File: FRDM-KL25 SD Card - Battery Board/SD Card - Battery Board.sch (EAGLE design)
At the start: 64 parts, among them J3 SSW-108-02-S-D, J4 SSW-110-02-S-D, J5 SSW-108-02-S-D, J6 SSW-106-02-S-D, U1 TPS63001, U2 TPS63002, U3 BQ27510DRZT-G3, U4 BQ24210DQCT

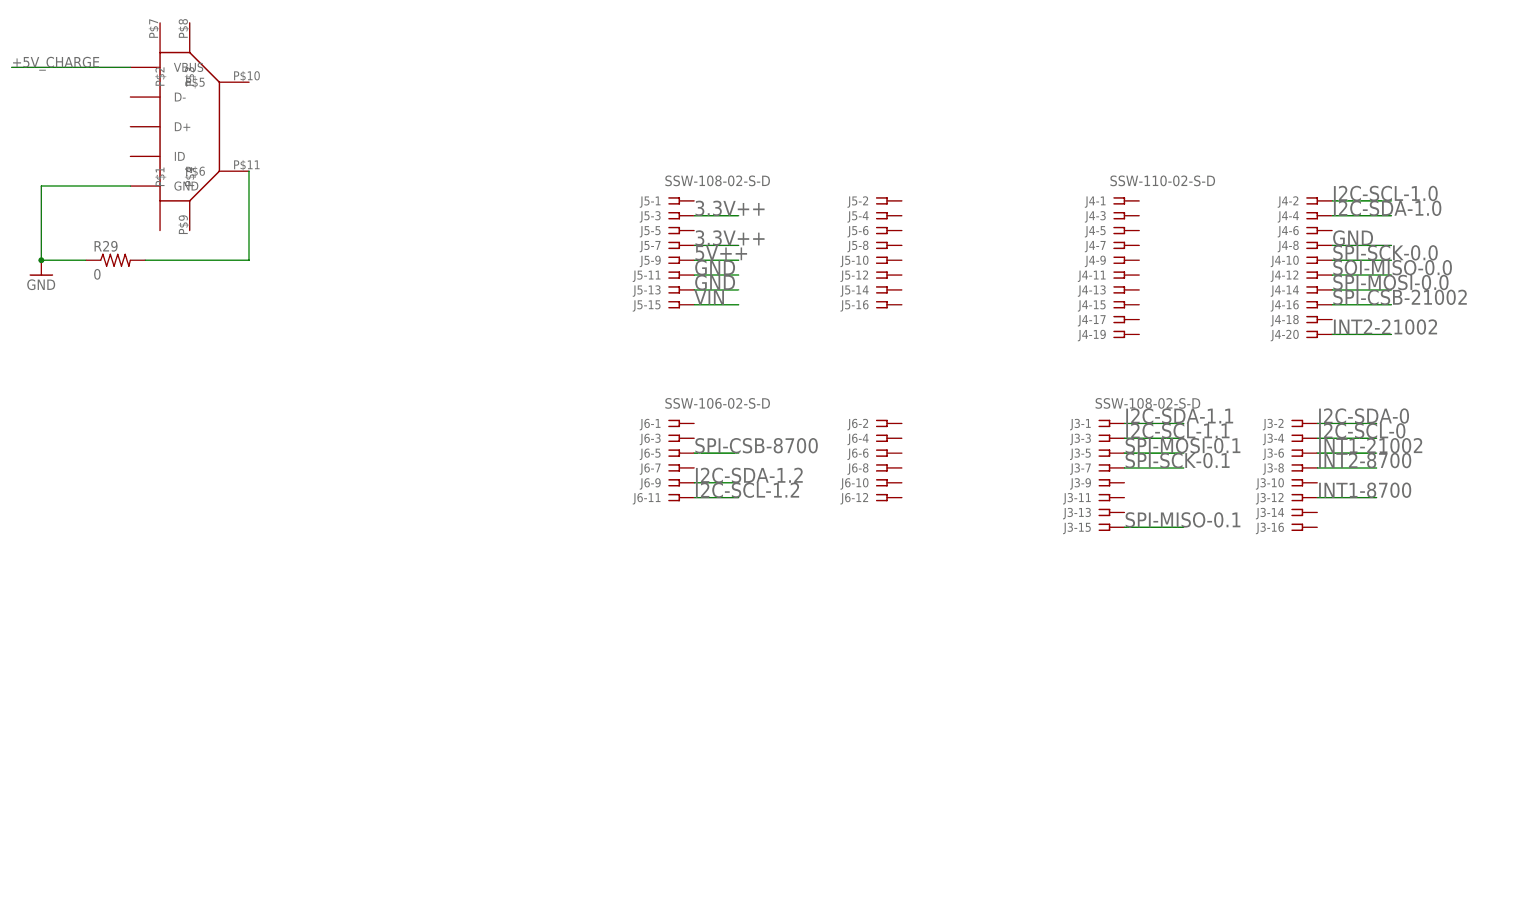
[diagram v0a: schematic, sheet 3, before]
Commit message: FRDM-KL25Z: LED names were updated to refelect the correct color, Layout of page 3 schematics was rearranged for better clarity. The the PCB the location of the SD card was placed in teh center, USB receptical was also placed in its needed location, SD card pull up resistors have been placed and connected, vias with 0.1 inch spacing have been used to ficilitate a header or test pins should that be needed.
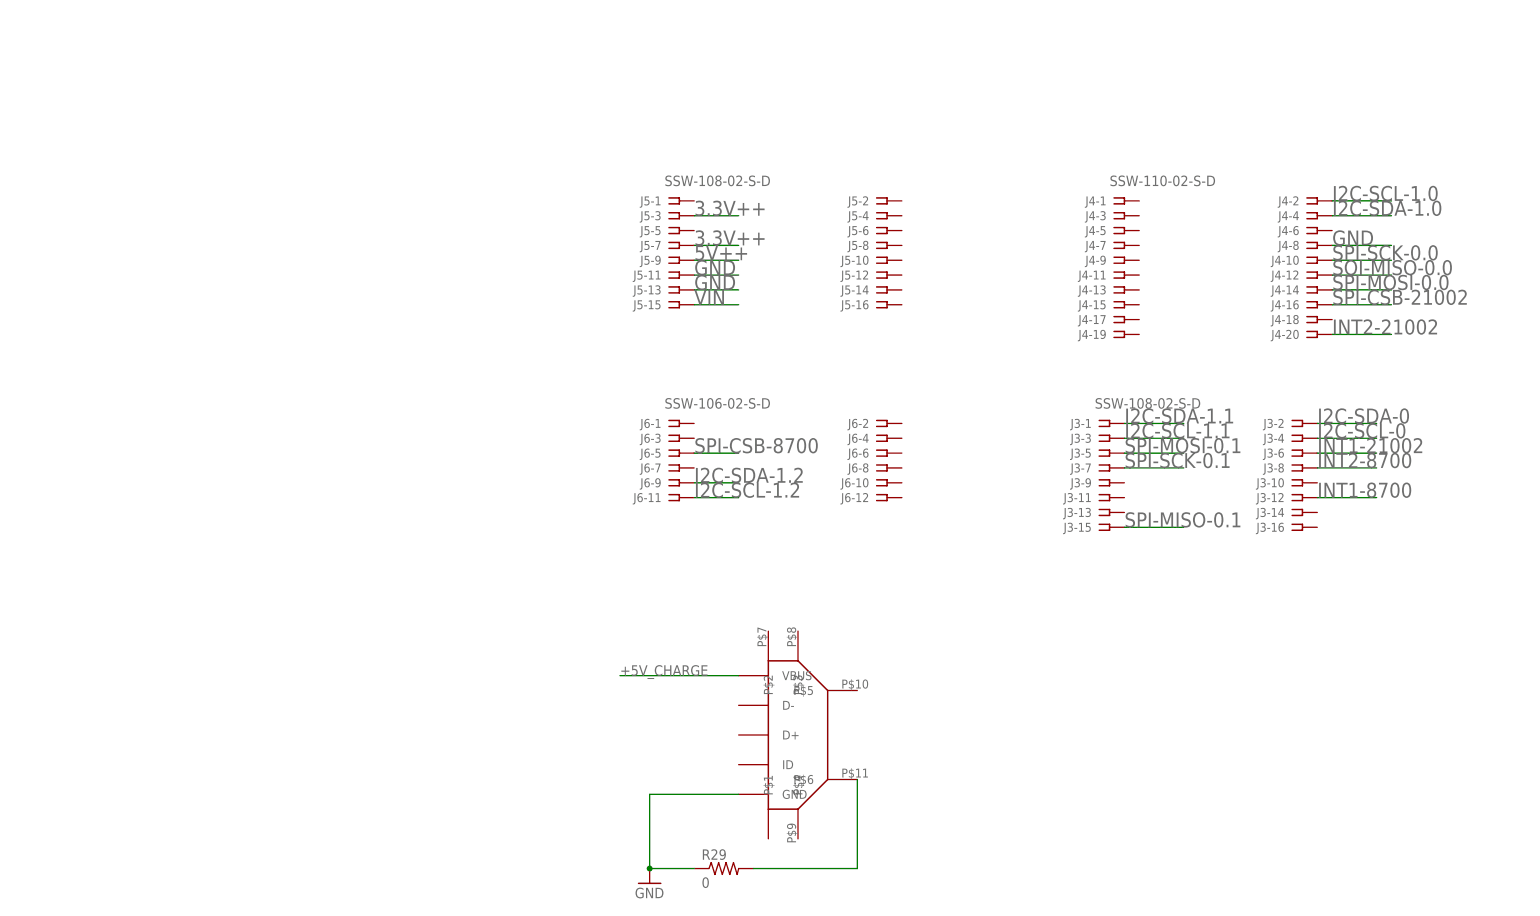
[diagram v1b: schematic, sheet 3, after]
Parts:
- D1: value Blue-LED -> Red-LED
- D2: value Green-LED -> Yellow-LED
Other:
- moved on the sheet: R29
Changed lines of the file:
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@@
 <part name="R12" library="Kas-Resistors" deviceset="RESISTOR" device="10K-62.5M-1%-50V" value="10k"/>
 <part name="R13" library="Kas-Resistors" deviceset="RESISTOR" device="10K-62.5M-1%-50V" value="10k"/>
-<part name="D2" library="Kas-Diodes-LEDs" deviceset="0.8X1.2" device="GREEN-3.3V-20M" value="Green-LED"/>
+<part name="D2" library="Kas-Diodes-LEDs" deviceset="0.8X1.2" device="GREEN-3.3V-20M" value="Yellow-LED"/>
 <part name="R14" library="Kas-Resistors" deviceset="RESISTOR" device="1K-63M-1%-50V-0402" value="1k"/>
 <part name="GND2" library="supply1" deviceset="GND" device=""/>
@@
 <part name="R25" library="Kas-Resistors" deviceset="RESISTOR" device="10K-62.5M-1%-50V" value="10k"/>
 <part name="R26" library="Kas-Resistors" deviceset="RESISTOR" device="1K-63M-1%-50V-0402" value="1k"/>
-<part name="D1" library="Kas-Diodes-LEDs" deviceset="0.8X1.2" device="BLUE-3.3V-20M" value="Blue-LED"/>
+<part name="D1" library="Kas-Diodes-LEDs" deviceset="0.8X1.2" device="BLUE-3.3V-20M" value="Red-LED"/>
 <part name="J1" library="Kas-Connectors" deviceset="SD_CARD_SLOT" device=""/>
 <part name="C2" library="Kas-Capacitors" deviceset="CAPACITOR" device="10U-X5R-20%-6.3V-0402" value="10uF"/>
@@
 <description>Connectors</description>
 <plain>
-<text x="76.2" y="-43.18" size="2.54" layer="101" ratio="14">NEED TO ADD BATTERY CONNECTION</text>
-<text x="190.5" y="30.48" size="2.54" layer="101" ratio="14">NEED TO ADD BATTERY CONNECTION</text>
-<text x="-68.58" y="35.56" size="2.54" layer="101" ratio="14">NEED TO ADD BATTERY CONNECTION</text>
-<text x="66.04" y="124.46" size="2.54" layer="101" ratio="14">NEED TO ADD BATTERY CONNECTION</text>
+<text x="-5.08" y="-38.1" size="2.54" layer="101" ratio="14">NEED TO ADD BATTERY CONNECTION</text>
+<text x="187.96" y="-38.1" size="2.54" layer="101" ratio="14">NEED TO ADD BATTERY CONNECTION</text>
+<text x="190.5" y="124.46" size="2.54" layer="101" ratio="14">NEED TO ADD BATTERY CONNECTION</text>
+<text x="7.62" y="127" size="2.54" layer="101" ratio="14">NEED TO ADD BATTERY CONNECTION</text>
 </plain>
 <instances>
@@
 <instance part="J6" gate="-11" x="50.8" y="45.72"/>
 <instance part="J6" gate="-12" x="86.36" y="45.72"/>
-<instance part="J2" gate="G$1" x="-27.94" y="111.76"/>
-<instance part="R29" gate="G$1" x="-45.72" y="86.36"/>
-<instance part="GND16" gate="1" x="-58.42" y="83.82"/>
+<instance part="J2" gate="G$1" x="76.2" y="7.62"/>
+<instance part="R29" gate="G$1" x="58.42" y="-17.78"/>
+<instance part="GND16" gate="1" x="45.72" y="-20.32"/>
 </instances>
 <busses>
@@
 <pinref part="J2" gate="G$1" pin="GND"/>
 <pinref part="GND16" gate="1" pin="GND"/>
-<wire x1="-43.18" y1="99.06" x2="-58.42" y2="99.06" width="0.1524" layer="91"/>
-<wire x1="-58.42" y1="99.06" x2="-58.42" y2="86.36" width="0.1524" layer="91"/>
-<wire x1="-50.8" y1="86.36" x2="-58.42" y2="86.36" width="0.1524" layer="91"/>
-<junction x="-58.42" y="86.36"/>
+<wire x1="60.96" y1="-5.08" x2="45.72" y2="-5.08" width="0.1524" layer="91"/>
+<wire x1="45.72" y1="-5.08" x2="45.72" y2="-17.78" width="0.1524" layer="91"/>
+<wire x1="53.34" y1="-17.78" x2="45.72" y2="-17.78" width="0.1524" layer="91"/>
+<junction x="45.72" y="-17.78"/>
 <pinref part="R29" gate="G$1" pin="1"/>
 </segment>
@@
 <segment>
 <pinref part="J2" gate="G$1" pin="VBUS"/>
-<wire x1="-43.18" y1="119.38" x2="-63.5" y2="119.38" width="0.1524" layer="91"/>
-<label x="-63.5" y="119.38" size="1.778" layer="95"/>
+<wire x1="60.96" y1="15.24" x2="40.64" y2="15.24" width="0.1524" layer="91"/>
+<label x="40.64" y="15.24" size="1.778" layer="95"/>
 </segment>
 </net>
@@
 <segment>
 <pinref part="J2" gate="G$1" pin="P$6"/>
-<wire x1="-22.86" y1="101.6" x2="-22.86" y2="86.36" width="0.1524" layer="91"/>
-<wire x1="-22.86" y1="86.36" x2="-40.64" y2="86.36" width="0.1524" layer="91"/>
+<wire x1="81.28" y1="-2.54" x2="81.28" y2="-17.78" width="0.1524" layer="91"/>
+<wire x1="81.28" y1="-17.78" x2="63.5" y2="-17.78" width="0.1524" layer="91"/>
 <pinref part="R29" gate="G$1" pin="2"/>
 </segment>

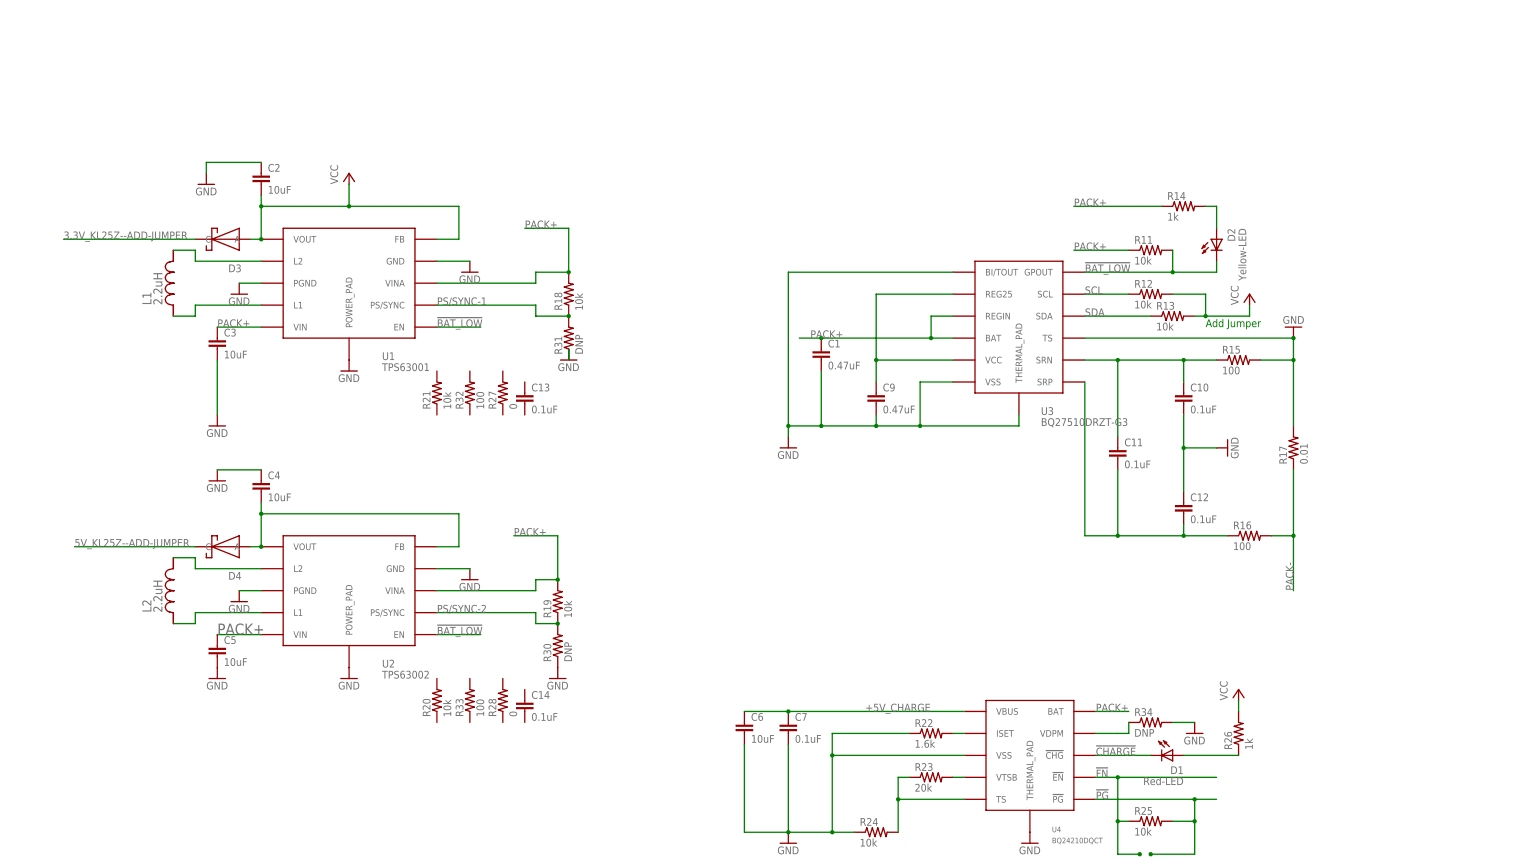
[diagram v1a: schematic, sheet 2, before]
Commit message: FRDM-KL26Z: Added 5V+ and changed VCC to 3V3+, moved battery section off PCB in preperation for branch
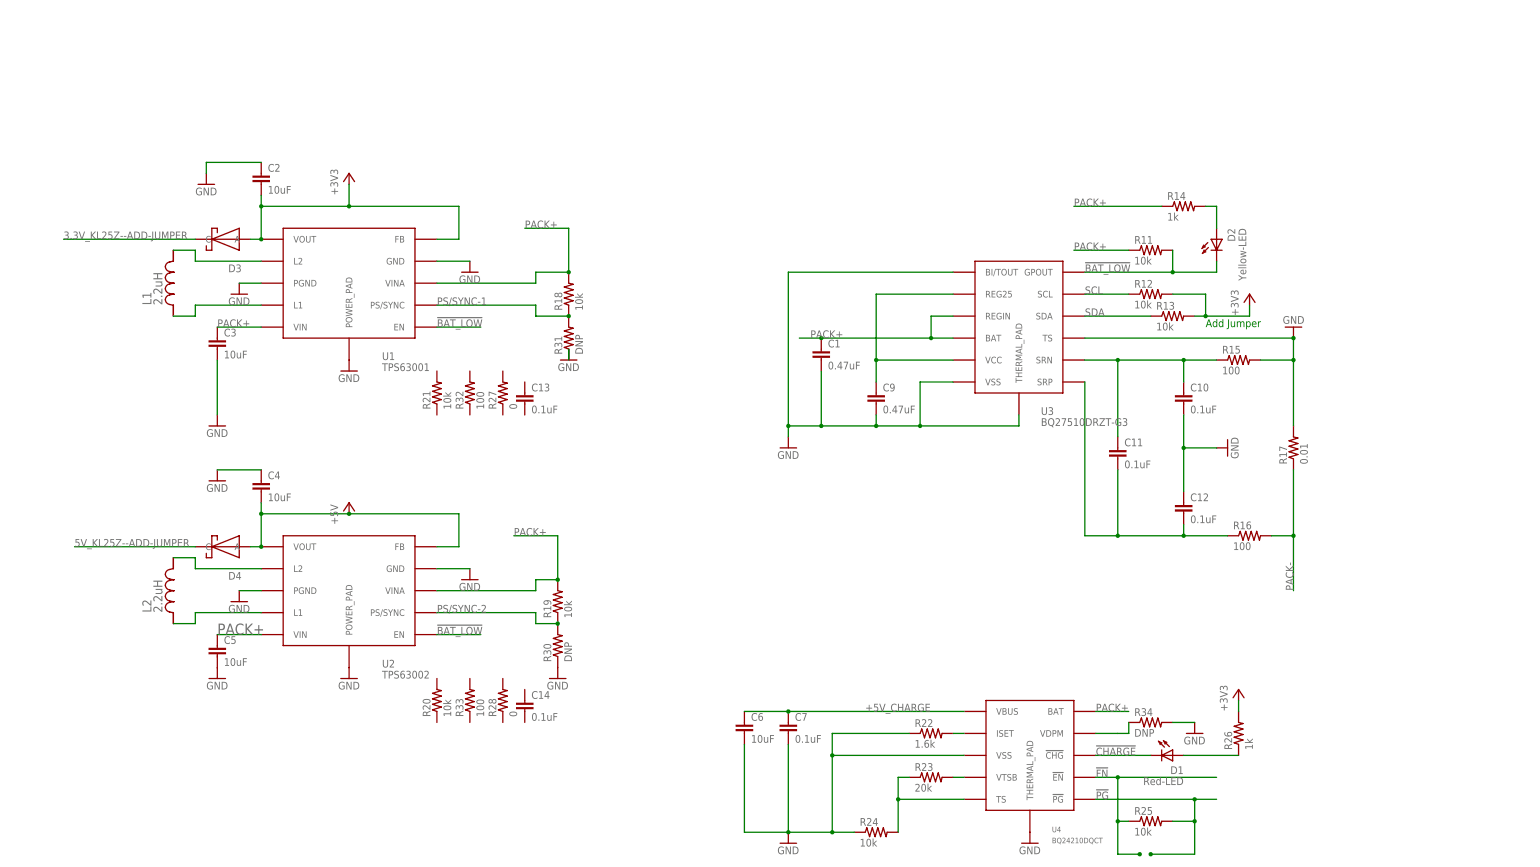
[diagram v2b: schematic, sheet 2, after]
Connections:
- net N$2 renamed +5V
- net VCC renamed +3V3
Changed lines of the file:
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@@
 <part name="C14" library="Kas-Capacitors" deviceset="CAPACITOR" device="0.1U-X7R-10%-25V" value="0.1uF"/>
 <part name="GND4" library="Kas-Pwr" deviceset="GND" device=""/>
-<part name="P+1" library="Kas-Pwr" deviceset="VCC" device=""/>
-<part name="P+2" library="Kas-Pwr" deviceset="VCC" device=""/>
+<part name="P+1" library="Kas-Pwr" deviceset="+3V3" device=""/>
+<part name="P+2" library="Kas-Pwr" deviceset="+3V3" device=""/>
 <part name="GND5" library="supply1" deviceset="GND" device=""/>
 <part name="GND6" library="supply1" deviceset="GND" device=""/>
@@
 <part name="GND15" library="supply1" deviceset="GND" device=""/>
 <part name="GND16" library="supply1" deviceset="GND" device=""/>
-<part name="P+3" library="Kas-Pwr" deviceset="VCC" device=""/>
-<part name="P+4" library="Kas-Pwr" deviceset="VCC" device=""/>
+<part name="P+3" library="Kas-Pwr" deviceset="+3V3" device=""/>
+<part name="P+4" library="Kas-Pwr" deviceset="+3V3" device=""/>
 <part name="GND17" library="supply1" deviceset="GND" device=""/>
 <part name="GND18" library="supply1" deviceset="GND" device=""/>
-<part name="P+5" library="Kas-Pwr" deviceset="VCC" device=""/>
+<part name="P+5" library="Kas-Pwr" deviceset="+3V3" device=""/>
 <part name="GND19" library="supply1" deviceset="GND" device=""/>
 <part name="J3" library="Kas-Connectors" deviceset="SSW-108-02-S-D" device=""/>
@@
 <part name="R34" library="Kas-Resistors" deviceset="RESISTOR" device="0402" value="DNP"/>
 <part name="GND20" library="supply1" deviceset="GND" device=""/>
+<part name="P+6" library="Kas-Pwr" deviceset="+5V" device=""/>
 </parts>
 <sheets>
@@
 <instance part="C8" gate="G$1" x="-17.78" y="45.72"/>
 <instance part="GND4" gate="1" x="-17.78" y="40.64"/>
-<instance part="P+1" gate="VCC" x="-17.78" y="55.88"/>
-<instance part="P+2" gate="VCC" x="53.34" y="99.06"/>
+<instance part="P+1" gate="G$1" x="-17.78" y="55.88"/>
+<instance part="P+2" gate="G$1" x="53.34" y="99.06"/>
 </instances>
 <busses>
@@
 </segment>
 </net>
-<net name="VCC" class="0">
+<net name="+3V3" class="0">
 <segment>
 <pinref part="J1" gate="G$1" pin="VDD"/>
@@
 <pinref part="C8" gate="G$1" pin="1"/>
 <wire x1="-17.78" y1="53.34" x2="-17.78" y2="50.8" width="0.1524" layer="91"/>
-<pinref part="P+1" gate="VCC" pin="VCC"/>
+<pinref part="P+1" gate="G$1" pin="+3V3"/>
 <junction x="-17.78" y="53.34"/>
 </segment>
@@
 <wire x1="71.12" y1="91.44" x2="78.74" y2="91.44" width="0.1524" layer="91"/>
 <junction x="78.74" y="91.44"/>
-<pinref part="P+2" gate="VCC" pin="VCC"/>
+<pinref part="P+2" gate="G$1" pin="+3V3"/>
 <wire x1="53.34" y1="96.52" x2="53.34" y2="91.44" width="0.1524" layer="91"/>
 <junction x="53.34" y="91.44"/>
@@
 <instance part="GND14" gate="1" x="-43.18" y="-5.08"/>
 <instance part="GND15" gate="1" x="-43.18" y="40.64"/>
-<instance part="P+3" gate="VCC" x="195.58" y="83.82"/>
-<instance part="P+4" gate="VCC" x="193.04" y="-7.62"/>
+<instance part="P+3" gate="G$1" x="195.58" y="83.82"/>
+<instance part="P+4" gate="G$1" x="193.04" y="-7.62"/>
 <instance part="GND17" gate="1" x="144.78" y="-43.18"/>
 <instance part="GND18" gate="1" x="88.9" y="-43.18"/>
-<instance part="P+5" gate="VCC" x="-12.7" y="111.76"/>
+<instance part="P+5" gate="G$1" x="-12.7" y="111.76"/>
 <instance part="GND19" gate="1" x="-12.7" y="-5.08"/>
 <instance part="R34" gate="G$1" x="172.72" y="-15.24"/>
 <instance part="GND20" gate="1" x="182.88" y="-17.78"/>
+<instance part="P+6" gate="1" x="-12.7" y="35.56"/>
 </instances>
 <busses>
@@
 </segment>
 </net>
-<net name="VCC" class="0">
+<net name="+3V3" class="0">
 <segment>
 <pinref part="R12" gate="G$1" pin="2"/>
@@
 <wire x1="195.58" y1="78.74" x2="195.58" y2="81.28" width="0.1524" layer="91"/>
 <junction x="185.42" y="78.74"/>
-<pinref part="P+3" gate="VCC" pin="VCC"/>
+<pinref part="P+3" gate="G$1" pin="+3V3"/>
 </segment>
 <segment>
 <pinref part="R26" gate="G$1" pin="2"/>
-<pinref part="P+4" gate="VCC" pin="VCC"/>
+<pinref part="P+4" gate="G$1" pin="+3V3"/>
 <wire x1="193.04" y1="-10.16" x2="193.04" y2="-12.7" width="0.1524" layer="91"/>
 </segment>
@@
 <pinref part="U1" gate="G$1" pin="FB"/>
 <wire x1="12.7" y1="96.52" x2="7.62" y2="96.52" width="0.1524" layer="91"/>
-<pinref part="P+5" gate="VCC" pin="VCC"/>
+<pinref part="P+5" gate="G$1" pin="+3V3"/>
 <wire x1="-12.7" y1="109.22" x2="-12.7" y2="104.14" width="0.1524" layer="91"/>
 <junction x="-12.7" y="104.14"/>
@@
 </segment>
 </net>
-<net name="N$2" class="0">
+<net name="N$3" class="0">
+<segment>
+<pinref part="U4" gate="G$1" pin="VDPM"/>
+<pinref part="R34" gate="G$1" pin="1"/>
+<wire x1="167.64" y1="-15.24" x2="167.64" y2="-17.78" width="0.1524" layer="91"/>
+<wire x1="167.64" y1="-17.78" x2="165.1" y2="-17.78" width="0.1524" layer="91"/>
+<wire x1="165.1" y1="-17.78" x2="160.02" y2="-17.78" width="0.1524" layer="91"/>
+</segment>
+</net>
+<net name="+5V" class="0">
 <segment>
 <wire x1="12.7" y1="33.02" x2="12.7" y2="25.4" width="0.1524" layer="91"/>
@@
 <wire x1="-33.02" y1="33.02" x2="-33.02" y2="25.4" width="0.1524" layer="91"/>
 <wire x1="-35.56" y1="25.4" x2="-33.02" y2="25.4" width="0.1524" layer="91"/>
-<wire x1="12.7" y1="33.02" x2="-33.02" y2="33.02" width="0.1524" layer="91"/>
+<wire x1="12.7" y1="33.02" x2="-12.7" y2="33.02" width="0.1524" layer="91"/>
 <junction x="-33.02" y="33.02"/>
-</segment>
-</net>
-<net name="N$3" class="0">
-<segment>
-<pinref part="U4" gate="G$1" pin="VDPM"/>
-<pinref part="R34" gate="G$1" pin="1"/>
-<wire x1="167.64" y1="-15.24" x2="167.64" y2="-17.78" width="0.1524" layer="91"/>
-<wire x1="167.64" y1="-17.78" x2="165.1" y2="-17.78" width="0.1524" layer="91"/>
-<wire x1="165.1" y1="-17.78" x2="160.02" y2="-17.78" width="0.1524" layer="91"/>
-</segment>
-</net>
+<pinref part="P+6" gate="1" pin="+5V"/>
+<wire x1="-12.7" y1="33.02" x2="-33.02" y2="33.02" width="0.1524" layer="91"/>
+<junction x="-12.7" y="33.02"/>
+</segment>
+</net>
